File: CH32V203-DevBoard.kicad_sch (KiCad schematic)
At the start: 40 parts, among them J1 USB_C_Receptacle_USB2.0_16P, J2 USB_C_Receptacle_USB2.0_16P, SW1 SW_Push, SW2 SW_Push, SW3 SW_Push, U1 CH32V203C8T6, U2 RT9080-33GJ5

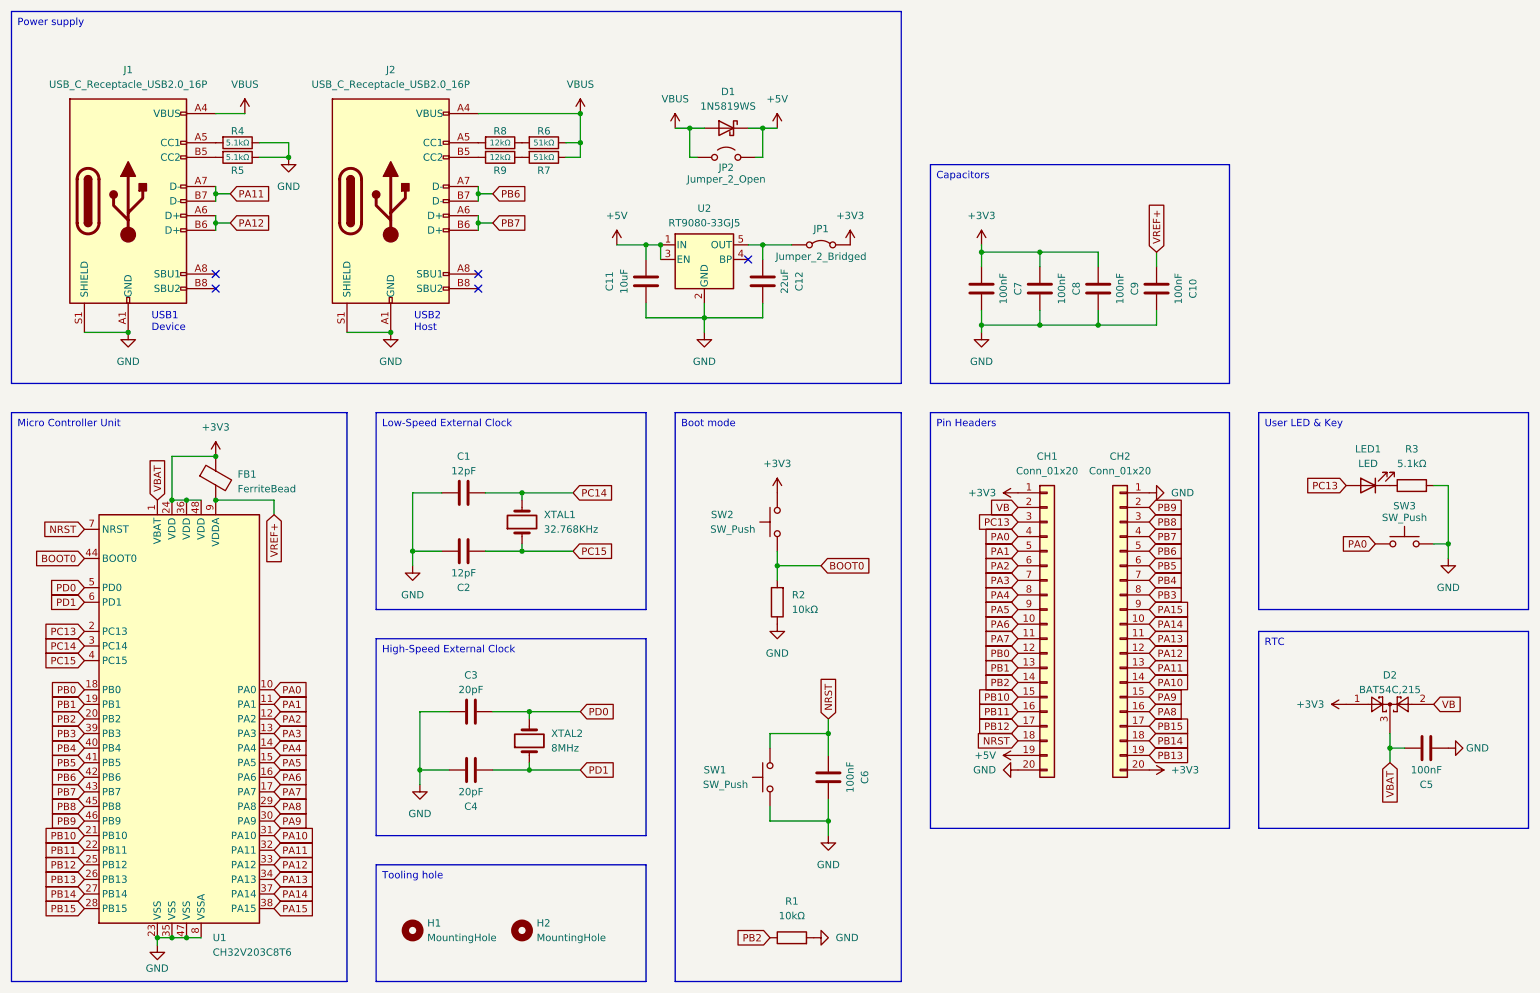
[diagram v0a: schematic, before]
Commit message: user key resistor fix
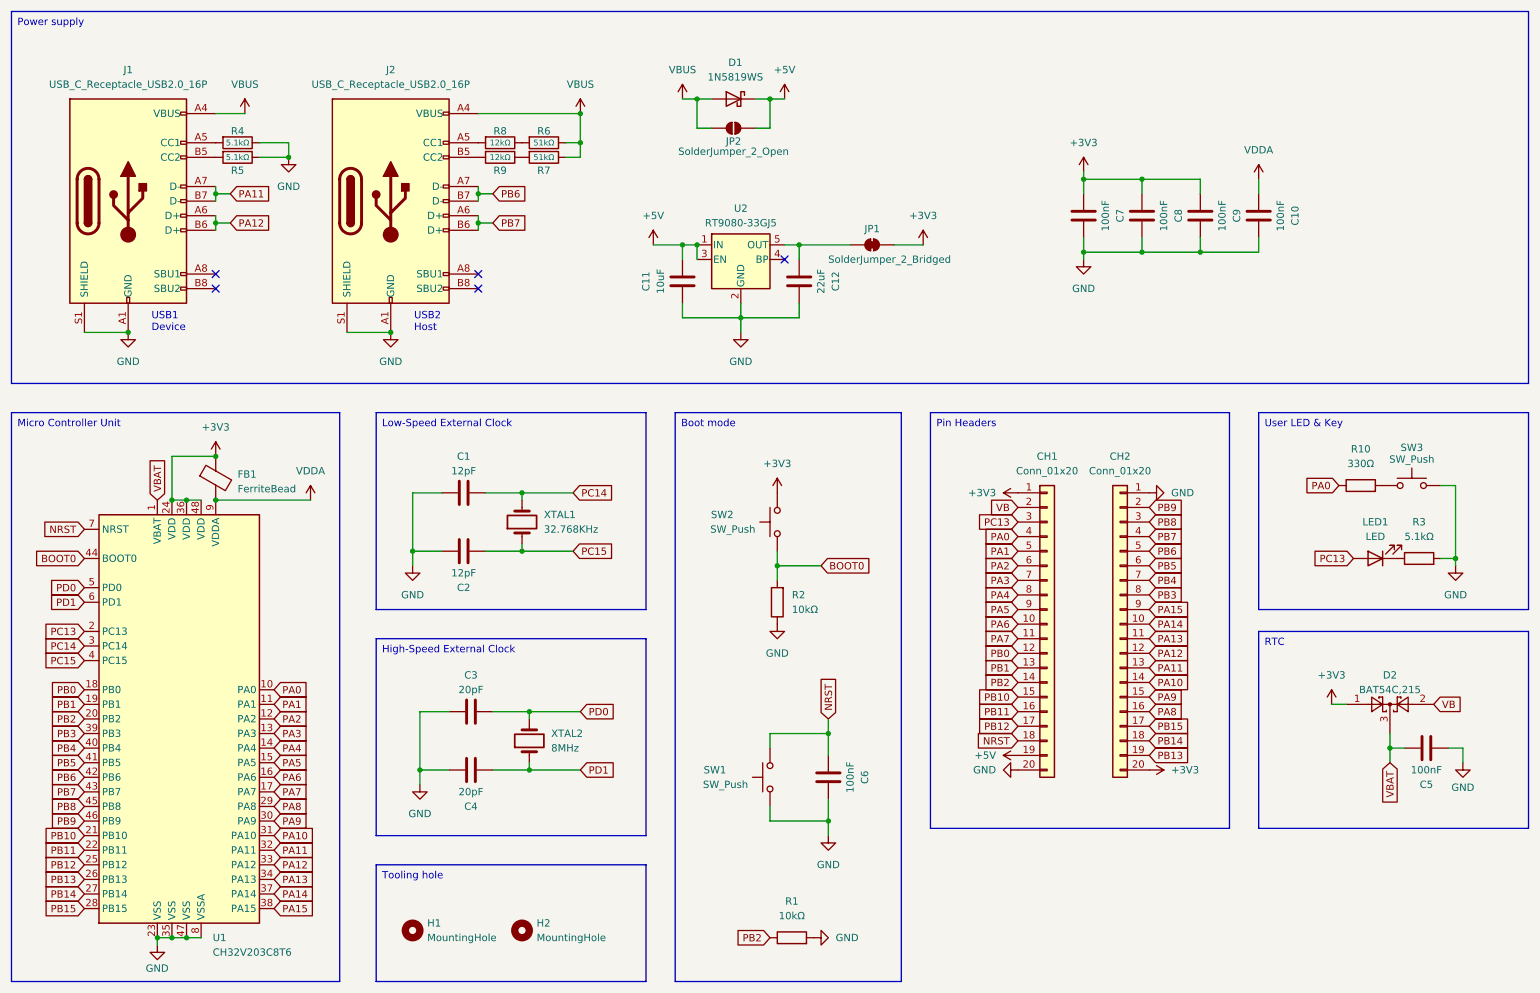
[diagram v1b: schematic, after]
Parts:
- added R10: 330Ω, Resistor_SMD:R_0402_1005Metric, symbol Device:R
- JP1: value Jumper_2_Bridged -> SolderJumper_2_Bridged; symbol Jumper:Jumper_2_Bridged -> Jumper:SolderJumper_2_Bridged
- JP2: value Jumper_2_Open -> SolderJumper_2_Open; symbol Jumper:Jumper_2_Open -> Jumper:SolderJumper_2_Open
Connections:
- net PA0: now also R10.1; no longer SW3.1
- net VREF+ renamed VDDA
- new net: R10.2, SW3.1
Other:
- moved on the sheet: C10, C11, C12, C7, C8, C9, D1, LED1, R3, U2

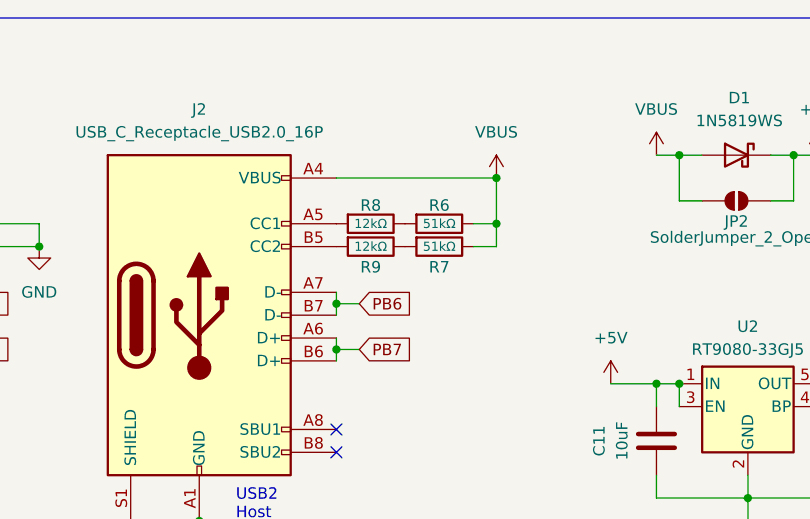
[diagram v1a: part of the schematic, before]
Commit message: cc resistor fix
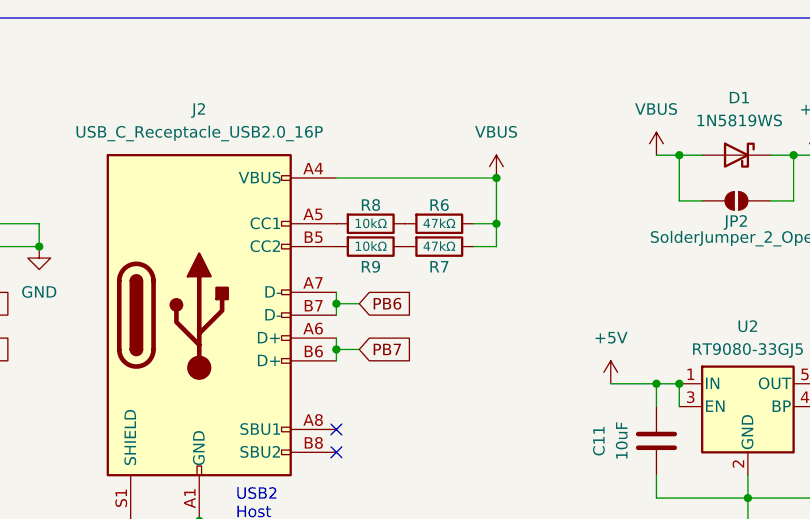
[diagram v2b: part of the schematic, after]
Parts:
- R6, R7: value 51kΩ -> 47kΩ; LCSC C25794 -> C25792
- R8, R9: value 12kΩ -> 10kΩ; LCSC C25752 -> C25744
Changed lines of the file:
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@@
 			)
 		)
-		(property "Value" "51kΩ"
+		(property "Value" "47kΩ"
 			(at 109.22 41.91 90)
 			(effects
@@
 			)
 		)
-		(property "LCSC" "C25794"
+		(property "LCSC" "C25792"
 			(at 109.22 41.91 90)
 			(effects
@@
 			)
 		)
-		(property "Value" "12kΩ"
+		(property "Value" "10kΩ"
 			(at 101.6 41.91 90)
 			(effects
@@
 			)
 		)
-		(property "LCSC" "C25752"
+		(property "LCSC" "C25744"
 			(at 101.6 41.91 90)
 			(effects
@@
 			)
 		)
-		(property "Value" "12kΩ"
+		(property "Value" "10kΩ"
 			(at 101.6 39.37 90)
 			(effects
@@
 			)
 		)
-		(property "LCSC" "C25752"
+		(property "LCSC" "C25744"
 			(at 101.6 39.37 90)
 			(effects
@@
 			)
 		)
-		(property "Value" "51kΩ"
+		(property "Value" "47kΩ"
 			(at 109.22 39.37 90)
 			(effects
@@
 			)
 		)
-		(property "LCSC" "C25794"
+		(property "LCSC" "C25792"
 			(at 109.22 39.37 90)
 			(effects

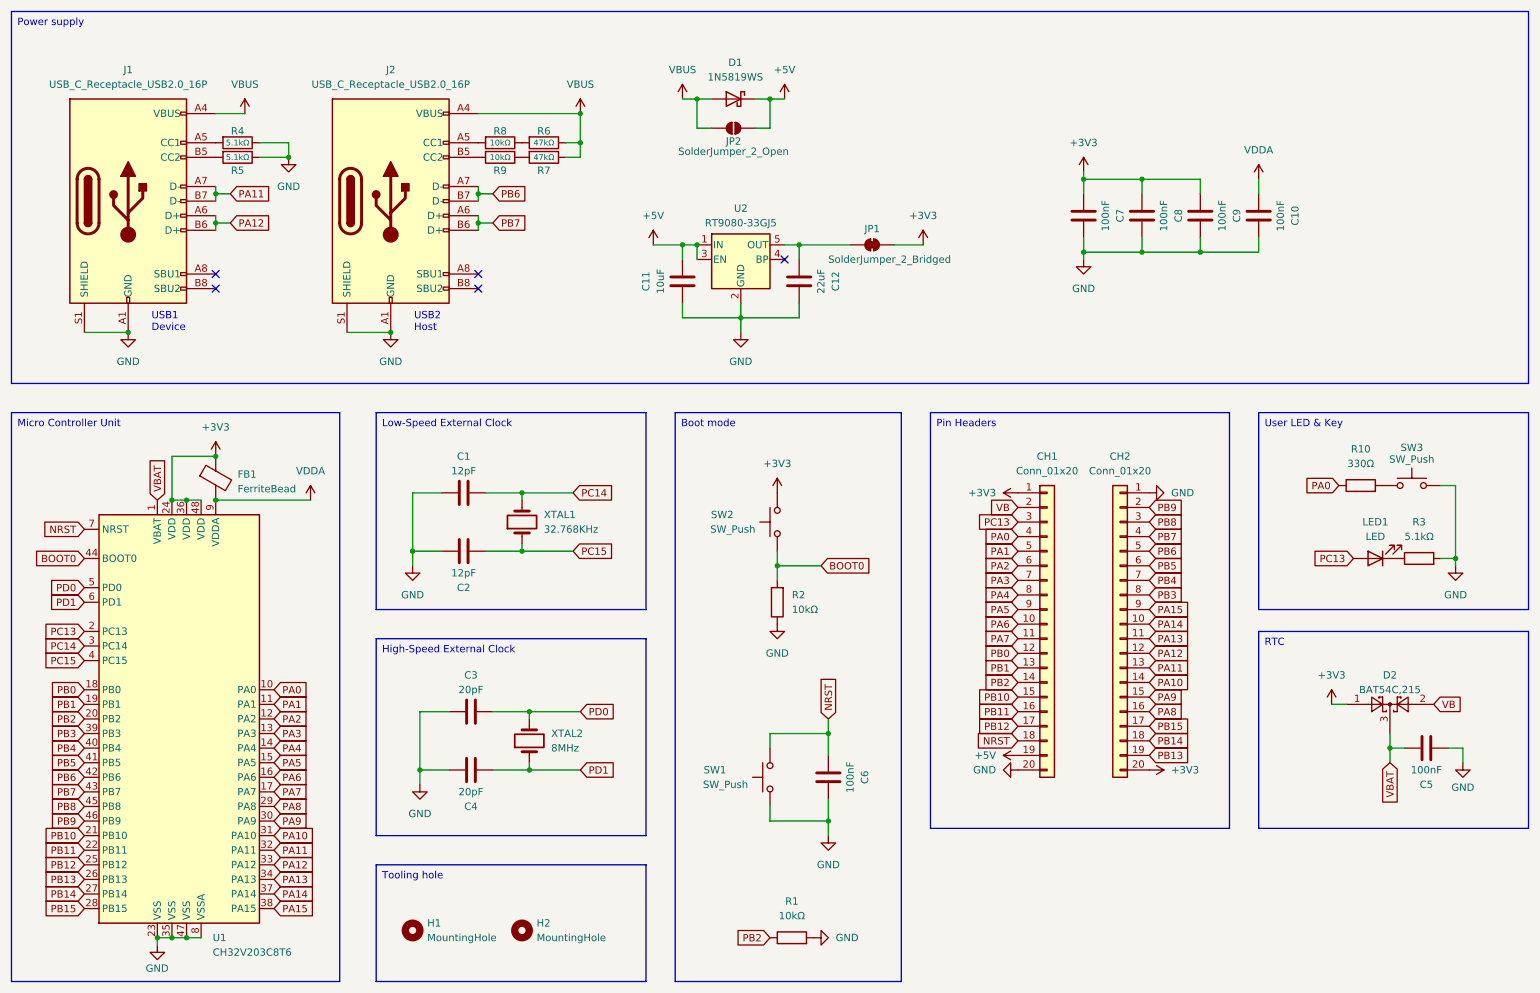
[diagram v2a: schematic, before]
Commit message: add host vbus switch
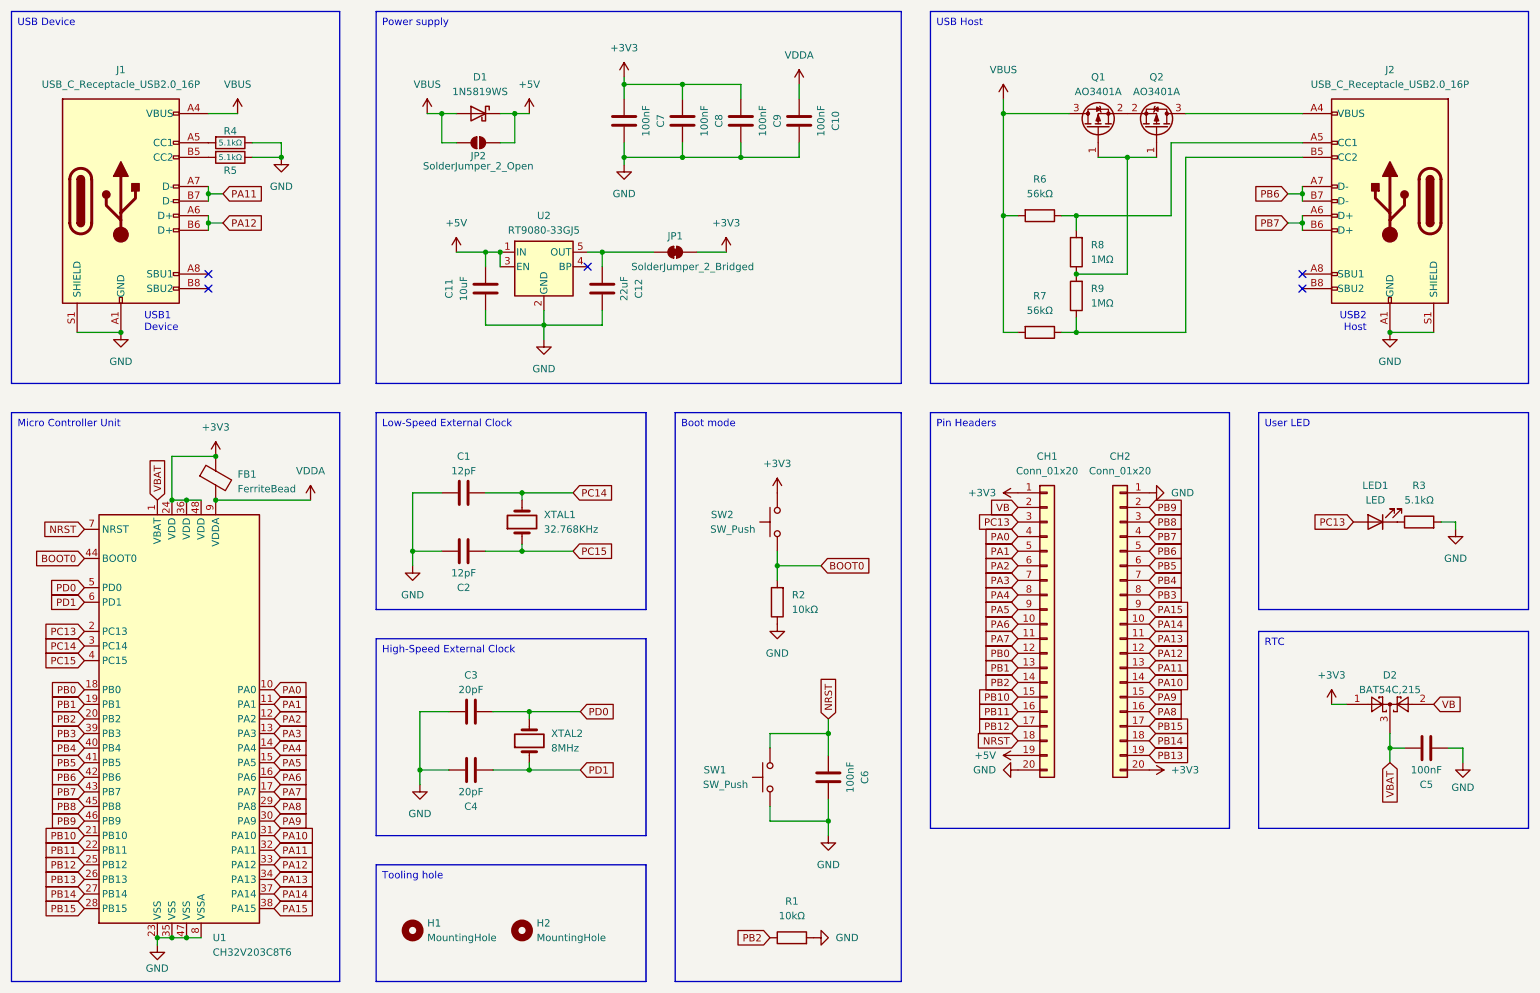
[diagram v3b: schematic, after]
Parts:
- removed R10: 330Ω, Resistor_SMD:R_0402_1005Metric, symbol Device:R
- removed SW3: SW_Push, Button_Switch_SMD:SW_SPST_PTS810, symbol Switch:SW_Push
- added Q1, Q2: AO3401A, Package_TO_SOT_SMD:SOT-23, symbol Transistor_FET:AO3401A
- R6, R7: value 47kΩ -> 56kΩ; footprint Resistor_SMD:R_0402_1005Metric -> Resistor_SMD:R_0603_1608Metric; LCSC C25792 -> C23206
- R8, R9: value 10kΩ -> 1MΩ; LCSC C25744 -> C26083
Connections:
- net VBUS: now also R6.2, R7.2, Q1.3 (D); no longer J2.A4 (VBUS), J2.A9 (VBUS), J2.B4 (VBUS), J2.B9 (VBUS), R6.1, R7.1
- net at R9.1: now also J2.B5 (CC2), R7.1; no longer R7.2
- net at R9.2: now also R8.1, Q1.1 (G), Q2.1 (G); no longer J2.B5 (CC2)
- net at J2.A5 (CC1), R8.2: now also R6.1
- new net: Q1.2 (S), Q2.2 (S)
- new net: J2.A4 (VBUS), J2.A9 (VBUS), J2.B4 (VBUS), J2.B9 (VBUS), Q2.3 (D)
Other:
- moved on the sheet: C10, C11, C12, C7, C8, C9, D1, J1, J2, JP1, JP2, LED1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

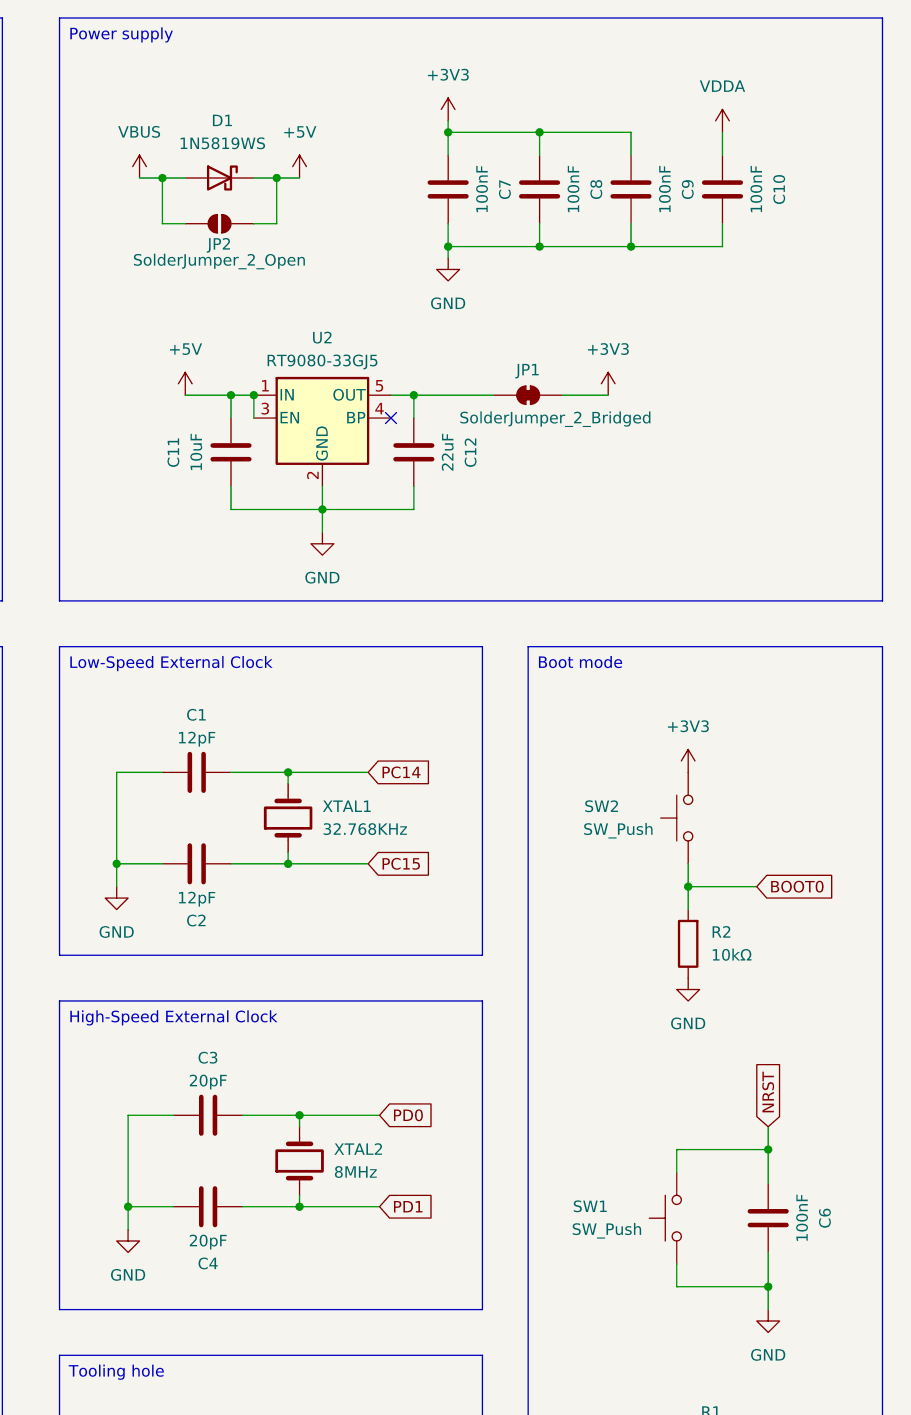
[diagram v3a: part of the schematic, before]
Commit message: crystal load capacitor fix
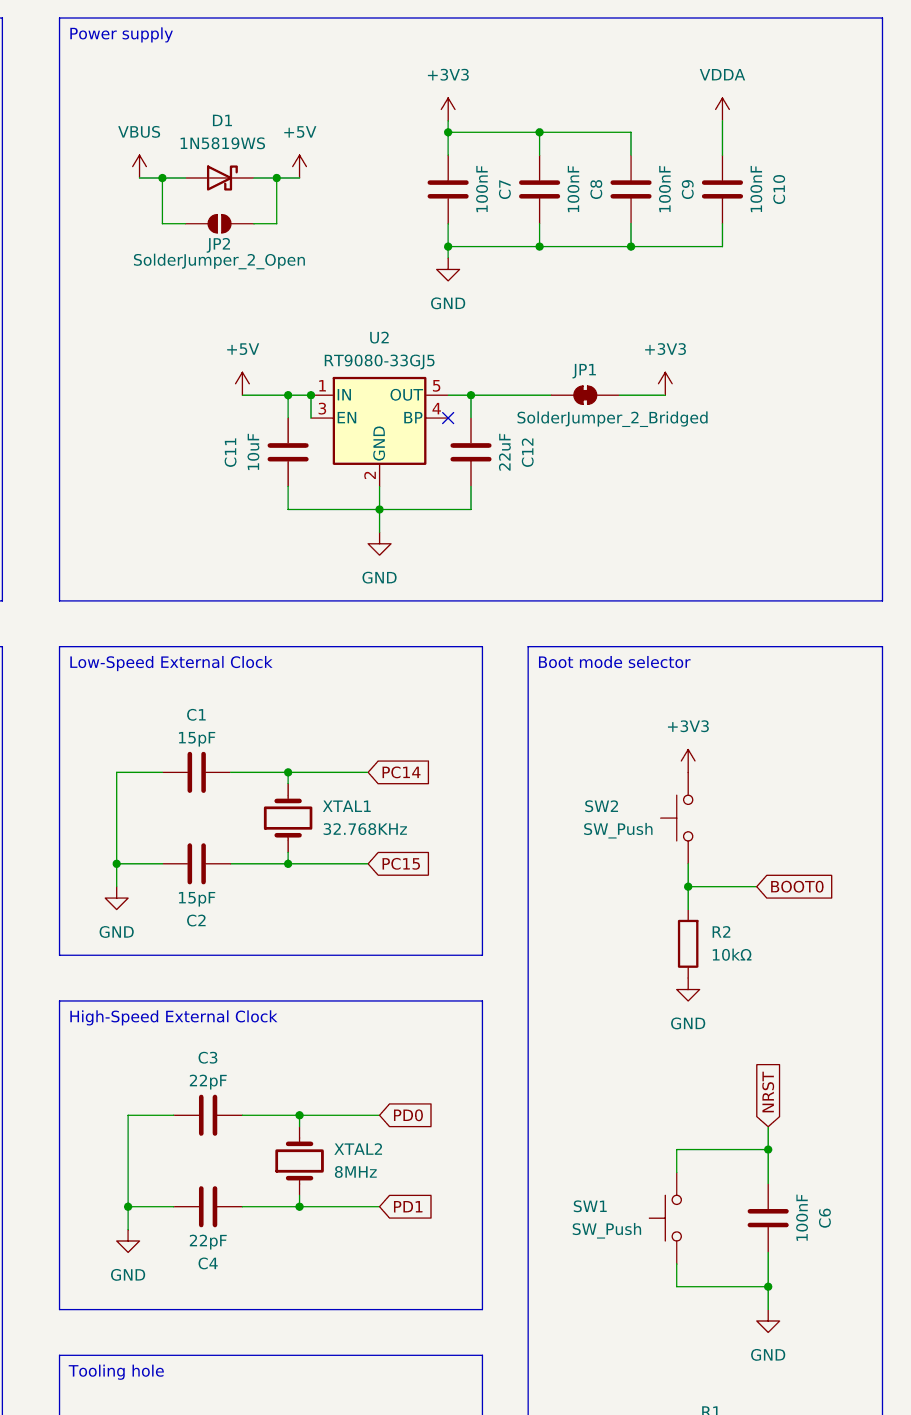
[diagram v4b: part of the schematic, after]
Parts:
- C1, C2: value 12pF -> 15pF; LCSC C1547 -> C1548
- C3, C4: value 20pF -> 22pF; LCSC C1554 -> C1555
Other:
- moved on the sheet: C11, C12, JP1, U2
